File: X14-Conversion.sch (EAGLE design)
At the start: 23 parts, among them P1 282837-2, P2 282837-2, P3 282837-2, U1 BUCK,LM2678S-ADJ

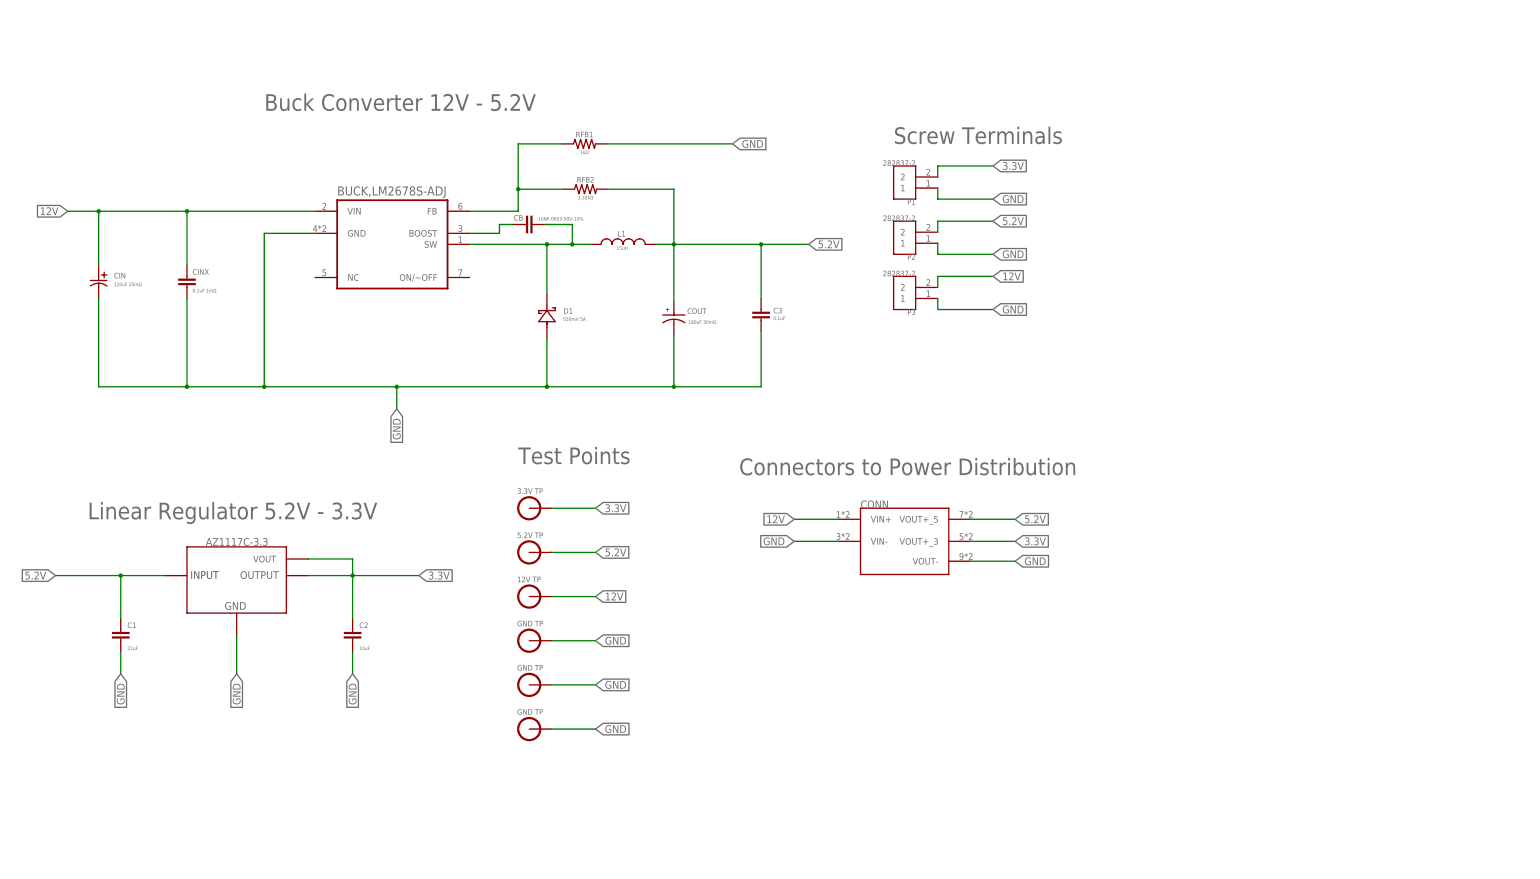
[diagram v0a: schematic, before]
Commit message: Change Output Capacitors
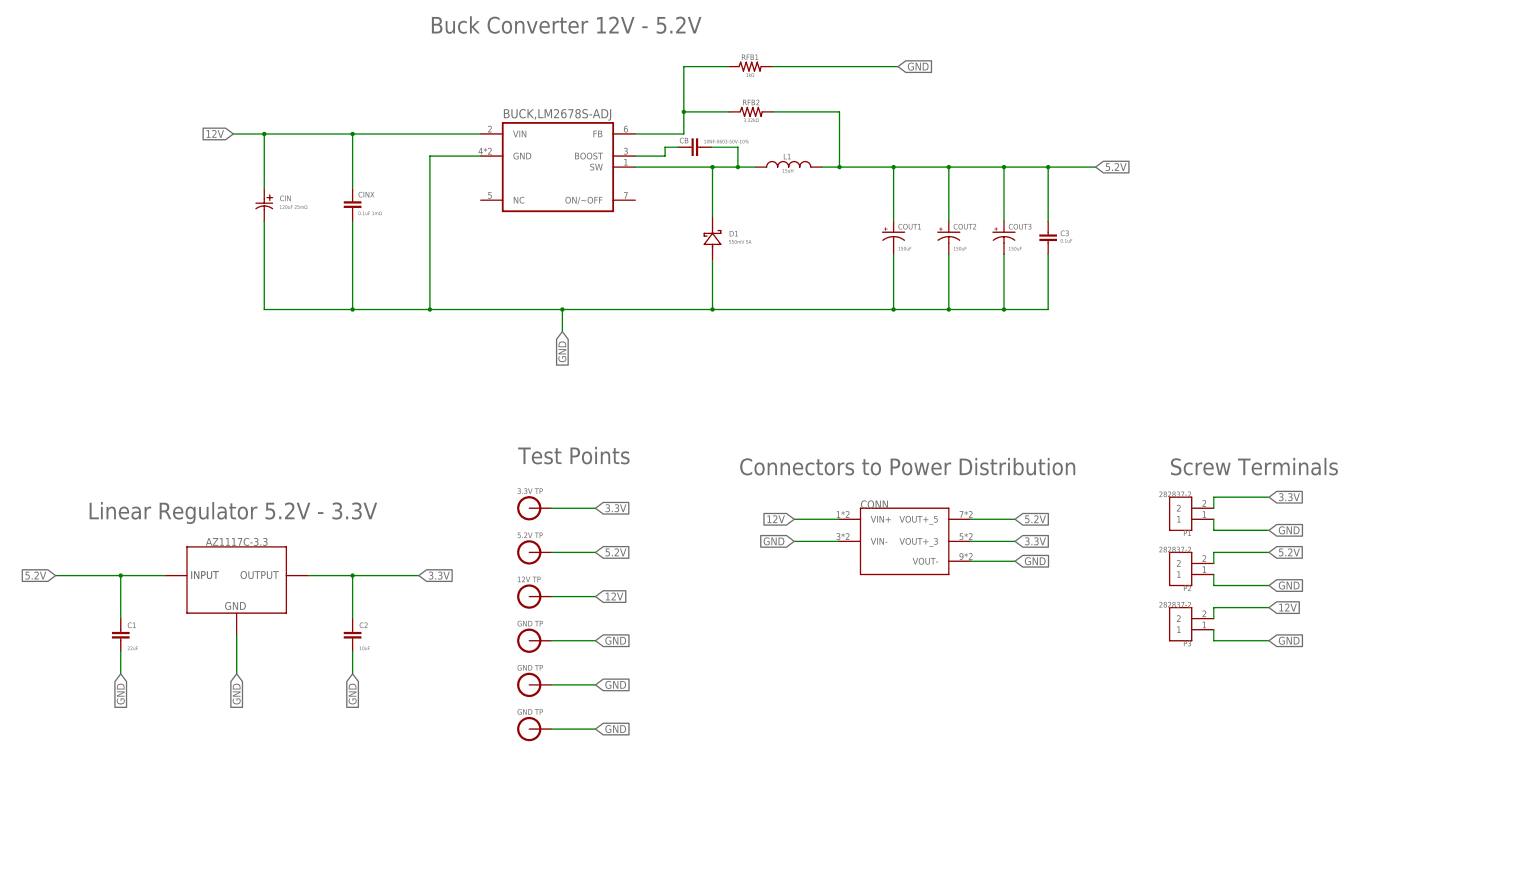
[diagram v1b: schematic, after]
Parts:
- removed COUT: 180uF 30mΩ, 16SVP180MX:16SVP180MX
- added COUT1, COUT2, COUT3: 150uF, CAP, Tantalum 150 uF - Kemet 2917 T491:C-TANTALUM(10UF_150UF)
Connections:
- net N$2 renamed SW
- net N$4 renamed CB
- net N$5 renamed FB
- net 3.3V: no longer AZ1117C.VOUT
- net 5.2V: now also COUT1.+, COUT2.+, COUT3.+; no longer COUT.1
- net GND: now also COUT1.-, COUT2.-, COUT3.-; no longer COUT.2
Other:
- moved on the sheet: C3, CB, CIN, CINX, D1, L1, P1, P2, P3, RFB1, RFB2

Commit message: fix board
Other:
- note added: "Fb Resistors Calculation: Vout = 5.2V; Vfb = 1.21V; Rfb1 = 1kΩ Vout = Vfb * ( 1 + Rfb2 / Rfb1) Rfb2 = Rfb1 * (Vout / Vfb - 1) Rfb2 = ~3.298kΩ = 3.32kΩ"
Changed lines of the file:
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@@
 <text x="-10.16" y="15.24" size="3.81" layer="95">Test Points</text>
 <text x="139.7" y="12.7" size="3.81" layer="95">Screw Terminals</text>
+<text x="139.7" y="91.44" size="2.54" layer="91">Fb Resistors Calculation:
+Vout = 5.2V; Vfb = 1.21V; Rfb1 = 1kΩ
+Vout = Vfb * ( 1 + Rfb2 / Rfb1)
+Rfb2 = Rfb1 * (Vout / Vfb - 1)
+Rfb2 = ~3.298kΩ = 3.32kΩ</text>
 </plain>
 <instances>
@@
 </drawing>
 <compatibility>
+<note version="6.3" minversion="6.2.2" severity="warning">
+Since Version 6.2.2 text objects can contain more than one line,
+which will not be processed correctly with this version.
+</note>
 <note version="8.2" severity="warning">
 Since Version 8.2, EAGLE supports online libraries. The ids

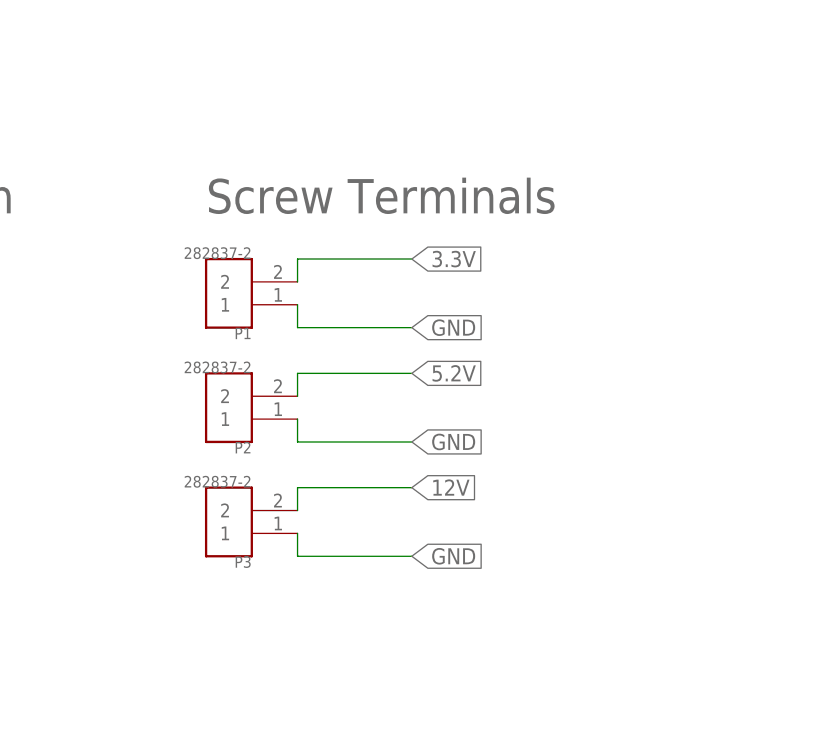
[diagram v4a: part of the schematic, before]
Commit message: Reduce board size
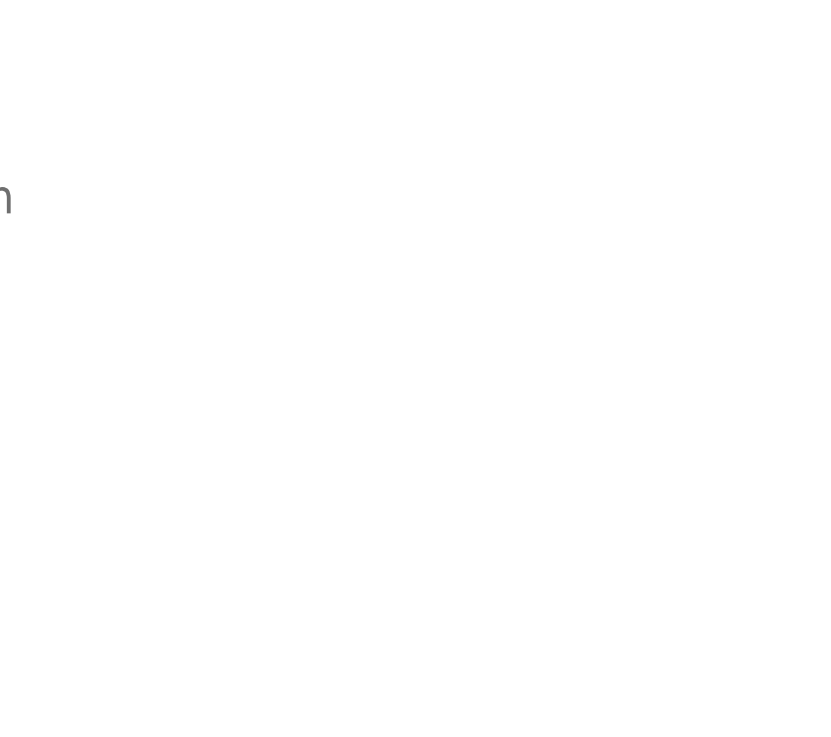
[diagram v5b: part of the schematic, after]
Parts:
- removed P1, P2, P3: 282837-2, ScrewPoints_282837-2:282837-2
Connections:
- net 12V: no longer P3.2
- net 3.3V: no longer P1.2
- net 5.2V: no longer P2.2
- net GND: no longer P1.1, P2.1, P3.1
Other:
- note removed: "Screw Terminals"
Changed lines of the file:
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@@
 <part name="U$6" library="testpoints" deviceset="GND_TESTPOINT" device=""/>
 <part name="U$7" library="testpoints" deviceset="GND_TESTPOINT" device=""/>
-<part name="P1" library="ScrewPoints_282837-2" deviceset="282837-2" device=""/>
-<part name="P2" library="ScrewPoints_282837-2" deviceset="282837-2" device=""/>
-<part name="P3" library="ScrewPoints_282837-2" deviceset="282837-2" device=""/>
 <part name="RFB2" library="SparkFun-Resistors" library_urn="urn:adsk.eagle:library:532" deviceset="3.3KOHM" device="-0603-1/10W-1%" package3d_urn="urn:adsk.eagle:package:39650/1" value="3.32kΩ"/>
 <part name="RFB1" library="SparkFun-Resistors" library_urn="urn:adsk.eagle:library:532" deviceset="1KOHM" device="-0603-1/10W-1%" package3d_urn="urn:adsk.eagle:package:39650/1" value="1kΩ"/>
@@
 <text x="-109.22" y="2.54" size="3.81" layer="95">Linear Regulator 5.2V - 3.3V</text>
 <text x="-10.16" y="15.24" size="3.81" layer="95">Test Points</text>
-<text x="139.7" y="12.7" size="3.81" layer="95">Screw Terminals</text>
 <text x="139.7" y="91.44" size="2.54" layer="91">Fb Resistors Calculation:
 Vout = 5.2V; Vfb = 1.21V; Rfb1 = 1kΩ
@@
 <instance part="U$6" gate="G$1" x="-7.62" y="-35.56" smashed="yes"/>
 <instance part="U$7" gate="G$1" x="-7.62" y="-45.72" smashed="yes"/>
-<instance part="P1" gate="G$1" x="142.24" y="2.54" smashed="yes" rot="R180">
-<attribute name="NAME" x="144.780559375" y="-0.00381875" size="1.271909375" layer="95" rot="R180"/>
-<attribute name="VALUE" x="144.78236875" y="8.914509375" size="1.274909375" layer="96" rot="R180"/>
-</instance>
-<instance part="P2" gate="G$1" x="142.24" y="-10.16" smashed="yes" rot="R180">
-<attribute name="NAME" x="144.780559375" y="-12.70381875" size="1.271909375" layer="95" rot="R180"/>
-<attribute name="VALUE" x="144.78236875" y="-3.785490625" size="1.274909375" layer="96" rot="R180"/>
-</instance>
-<instance part="P3" gate="G$1" x="142.24" y="-22.86" smashed="yes" rot="R180">
-<attribute name="NAME" x="144.780559375" y="-25.40381875" size="1.271909375" layer="95" rot="R180"/>
-<attribute name="VALUE" x="144.78236875" y="-16.485490625" size="1.274909375" layer="96" rot="R180"/>
-</instance>
 <instance part="RFB2" gate="G$1" x="43.434" y="96.266" smashed="yes">
 <attribute name="NAME" x="43.434" y="97.79" size="1.27" layer="95" align="bottom-center"/>
@@
 </segment>
 <segment>
-<pinref part="P2" gate="G$1" pin="1"/>
-<wire x1="149.86" y1="-10.16" x2="149.86" y2="-12.7" width="0.1524" layer="91"/>
-<wire x1="149.86" y1="-12.7" x2="162.56" y2="-12.7" width="0.1524" layer="91"/>
-<label x="162.56" y="-12.7" size="1.778" layer="95" xref="yes"/>
-</segment>
-<segment>
-<pinref part="P3" gate="G$1" pin="1"/>
-<wire x1="149.86" y1="-22.86" x2="149.86" y2="-25.4" width="0.1524" layer="91"/>
-<wire x1="149.86" y1="-25.4" x2="162.56" y2="-25.4" width="0.1524" layer="91"/>
-<label x="162.56" y="-25.4" size="1.778" layer="95" xref="yes"/>
-</segment>
-<segment>
-<wire x1="149.86" y1="0" x2="162.56" y2="0" width="0.1524" layer="91"/>
-<label x="162.56" y="0" size="1.778" layer="95" xref="yes"/>
-<pinref part="P1" gate="G$1" pin="1"/>
-<wire x1="149.86" y1="0" x2="149.86" y2="2.54" width="0.1524" layer="91"/>
-</segment>
-<segment>
 <pinref part="CONN" gate="G$1" pin="VIN-"/>
 <wire x1="63.5" y1="-2.54" x2="53.34" y2="-2.54" width="0.1524" layer="91"/>
@@
 <wire x1="-2.54" y1="5.08" x2="7.62" y2="5.08" width="0.1524" layer="91"/>
 <label x="7.62" y="5.08" size="1.778" layer="95" xref="yes"/>
-</segment>
-<segment>
-<pinref part="P1" gate="G$1" pin="2"/>
-<wire x1="149.86" y1="5.08" x2="149.86" y2="7.62" width="0.1524" layer="91"/>
-<wire x1="149.86" y1="7.62" x2="162.56" y2="7.62" width="0.1524" layer="91"/>
-<label x="162.56" y="7.62" size="1.778" layer="95" xref="yes"/>
 </segment>
 <segment>
@@
 </segment>
 <segment>
-<wire x1="149.86" y1="-5.08" x2="162.56" y2="-5.08" width="0.1524" layer="91"/>
-<label x="162.56" y="-5.08" size="1.778" layer="95" xref="yes"/>
-<pinref part="P2" gate="G$1" pin="2"/>
-<wire x1="149.86" y1="-7.62" x2="149.86" y2="-5.08" width="0.1524" layer="91"/>
-</segment>
-<segment>
 <pinref part="CONN" gate="G$1" pin="VOUT+_5"/>
 <wire x1="93.98" y1="2.54" x2="104.14" y2="2.54" width="0.1524" layer="91"/>
@@
 </segment>
 <segment>
-<wire x1="149.86" y1="-17.78" x2="162.56" y2="-17.78" width="0.1524" layer="91"/>
-<label x="162.56" y="-17.78" size="1.778" layer="95" xref="yes"/>
-<pinref part="P3" gate="G$1" pin="2"/>
-<wire x1="149.86" y1="-17.78" x2="149.86" y2="-20.32" width="0.1524" layer="91"/>
-</segment>
-<segment>

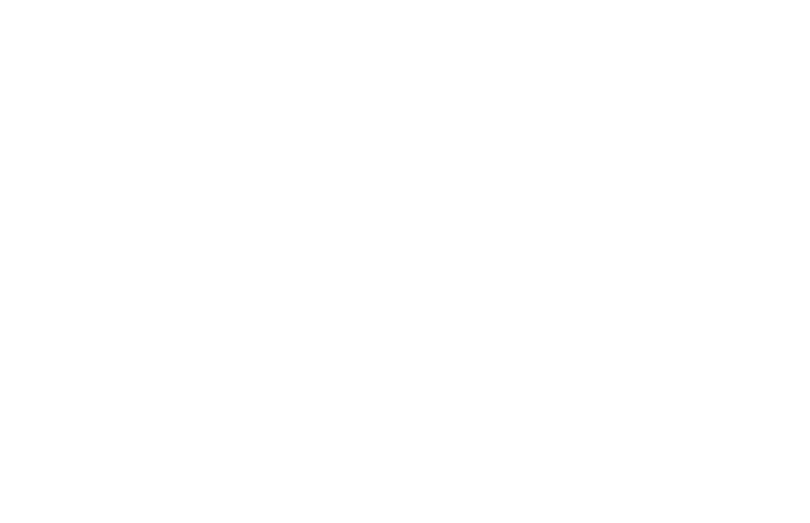
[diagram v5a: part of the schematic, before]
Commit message: add 1x2 headers to board
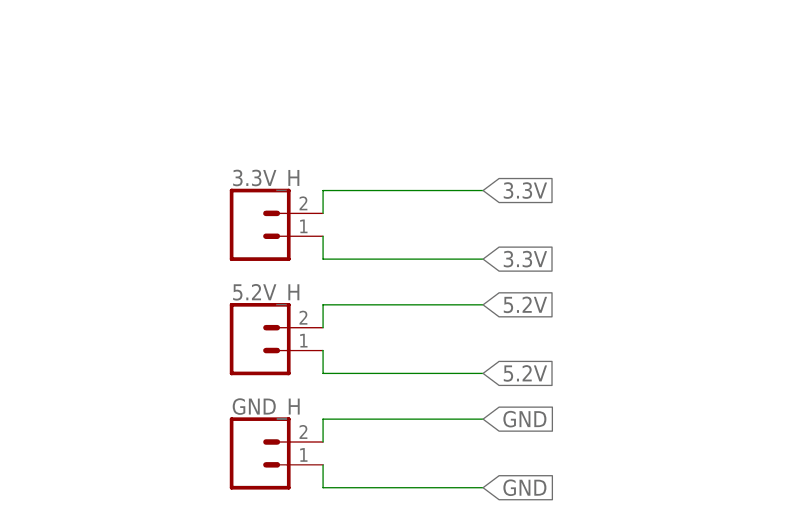
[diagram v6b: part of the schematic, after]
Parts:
- added 3.3V_H, 5.2V_H, GND_H: (no value), SparkFun-Connectors:CONN_02
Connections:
- net 3.3V: now also 3.3V_H.1, 3.3V_H.2
- net 5.2V: now also 5.2V_H.1, 5.2V_H.2
- net GND: now also GND_H.1, GND_H.2
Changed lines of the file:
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@@
 <part name="COUT2" library="CAP, Tantalum 150 uF - Kemet 2917 T491" deviceset="C-TANTALUM(10UF_150UF)" device="" package3d_urn="urn:adsk.eagle:package:25131320/3" value="150uF"/>
 <part name="COUT3" library="CAP, Tantalum 150 uF - Kemet 2917 T491" deviceset="C-TANTALUM(10UF_150UF)" device="" package3d_urn="urn:adsk.eagle:package:25131320/3" value="150uF"/>
+<part name="3.3V_H" library="SparkFun-Connectors" library_urn="urn:adsk.eagle:library:513" deviceset="CONN_02" device="" package3d_urn="urn:adsk.eagle:package:38039/1"/>
+<part name="5.2V_H" library="SparkFun-Connectors" library_urn="urn:adsk.eagle:library:513" deviceset="CONN_02" device="" package3d_urn="urn:adsk.eagle:package:38039/1"/>
+<part name="GND_H" library="SparkFun-Connectors" library_urn="urn:adsk.eagle:library:513" deviceset="CONN_02" device="" package3d_urn="urn:adsk.eagle:package:38039/1"/>
 </parts>
 <sheets>
@@
 <attribute name="NAME" x="102.616" y="69.215" size="1.27" layer="95"/>
 <attribute name="VALUE" x="102.616" y="64.389" size="0.8128" layer="96"/>
+</instance>
+<instance part="3.3V_H" gate="G$1" x="58.42" y="-48.26" smashed="yes">
+<attribute name="VALUE" x="55.88" y="-53.086" size="1.778" layer="96" font="vector"/>
+<attribute name="NAME" x="55.88" y="-42.672" size="1.778" layer="95" font="vector"/>
+</instance>
+<instance part="5.2V_H" gate="G$1" x="58.42" y="-60.96" smashed="yes">
+<attribute name="VALUE" x="55.88" y="-65.786" size="1.778" layer="96" font="vector"/>
+<attribute name="NAME" x="55.88" y="-55.372" size="1.778" layer="95" font="vector"/>
+</instance>
+<instance part="GND_H" gate="G$1" x="58.42" y="-73.66" smashed="yes">
+<attribute name="VALUE" x="55.88" y="-78.486" size="1.778" layer="96" font="vector"/>
+<attribute name="NAME" x="55.88" y="-68.072" size="1.778" layer="95" font="vector"/>
 </instance>
 </instances>
@@
 <label x="104.14" y="-7.112" size="1.778" layer="95" xref="yes"/>
 </segment>
+<segment>
+<pinref part="GND_H" gate="G$1" pin="2"/>
+<wire x1="66.04" y1="-71.12" x2="66.04" y2="-68.58" width="0.1524" layer="91"/>
+<wire x1="66.04" y1="-68.58" x2="83.82" y2="-68.58" width="0.1524" layer="91"/>
+<label x="83.82" y="-68.58" size="1.778" layer="95" xref="yes"/>
+</segment>
+<segment>
+<pinref part="GND_H" gate="G$1" pin="1"/>
+<wire x1="66.04" y1="-73.66" x2="66.04" y2="-76.2" width="0.1524" layer="91"/>
+<wire x1="66.04" y1="-76.2" x2="83.82" y2="-76.2" width="0.1524" layer="91"/>
+<label x="83.82" y="-76.2" size="1.778" layer="95" xref="yes"/>
+</segment>
 </net>
 <net name="3.3V" class="0">
@@
 <wire x1="93.98" y1="-2.54" x2="104.14" y2="-2.54" width="0.1524" layer="91"/>
 <label x="104.14" y="-2.54" size="1.778" layer="95" xref="yes"/>
+</segment>
+<segment>
+<pinref part="3.3V_H" gate="G$1" pin="2"/>
+<wire x1="66.04" y1="-45.72" x2="66.04" y2="-43.18" width="0.1524" layer="91"/>
+<wire x1="66.04" y1="-43.18" x2="83.82" y2="-43.18" width="0.1524" layer="91"/>
+<label x="83.82" y="-43.18" size="1.778" layer="95" xref="yes"/>
+</segment>
+<segment>
+<pinref part="3.3V_H" gate="G$1" pin="1"/>
+<wire x1="66.04" y1="-48.26" x2="66.04" y2="-50.8" width="0.1524" layer="91"/>
+<wire x1="66.04" y1="-50.8" x2="83.82" y2="-50.8" width="0.1524" layer="91"/>
+<label x="83.82" y="-50.8" size="1.778" layer="95" xref="yes"/>
 </segment>
 </net>
@@
 <label x="104.14" y="2.54" size="1.778" layer="95" xref="yes"/>
 </segment>
+<segment>
+<pinref part="5.2V_H" gate="G$1" pin="2"/>
+<wire x1="66.04" y1="-58.42" x2="66.04" y2="-55.88" width="0.1524" layer="91"/>
+<wire x1="66.04" y1="-55.88" x2="83.82" y2="-55.88" width="0.1524" layer="91"/>
+<label x="83.82" y="-55.88" size="1.778" layer="95" xref="yes"/>
+</segment>
+<segment>
+<pinref part="5.2V_H" gate="G$1" pin="1"/>
+<wire x1="66.04" y1="-60.96" x2="66.04" y2="-63.5" width="0.1524" layer="91"/>
+<wire x1="66.04" y1="-63.5" x2="83.82" y2="-63.5" width="0.1524" layer="91"/>
+<label x="83.82" y="-63.5" size="1.778" layer="95" xref="yes"/>
+</segment>
 </net>
